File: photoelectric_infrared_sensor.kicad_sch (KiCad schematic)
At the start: 37 parts

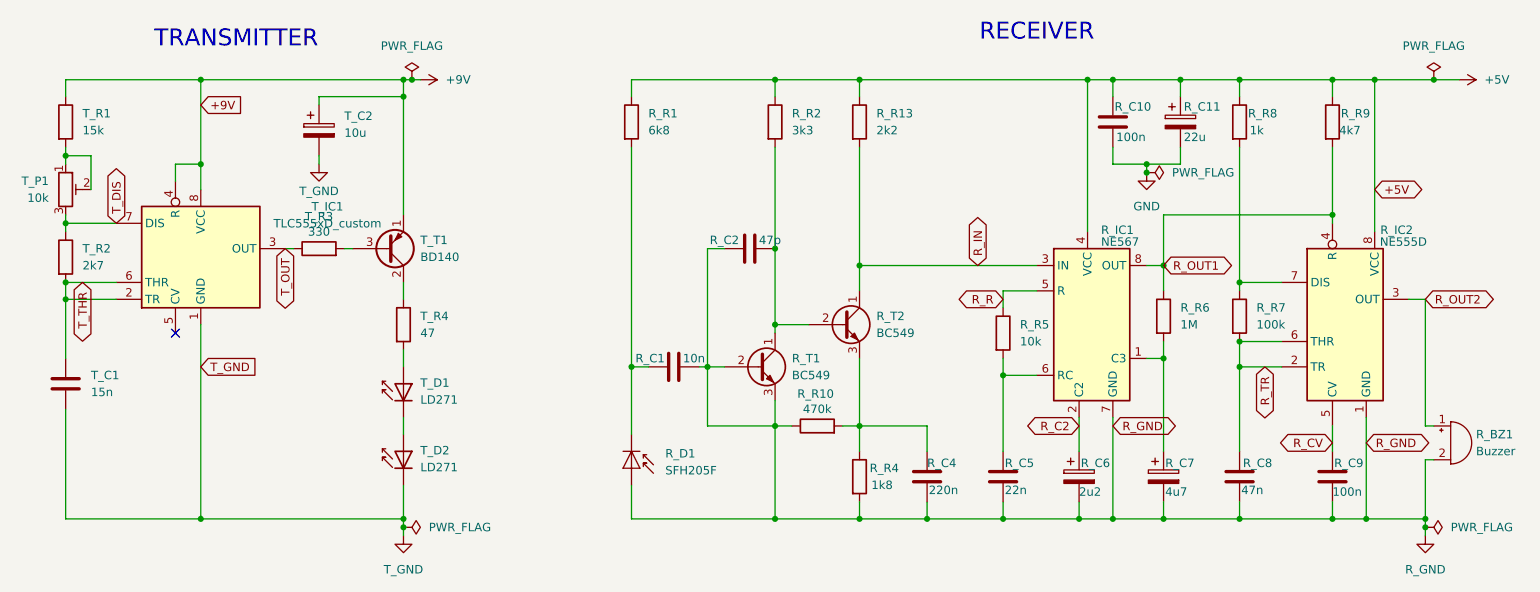
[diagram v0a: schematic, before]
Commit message: added BOM
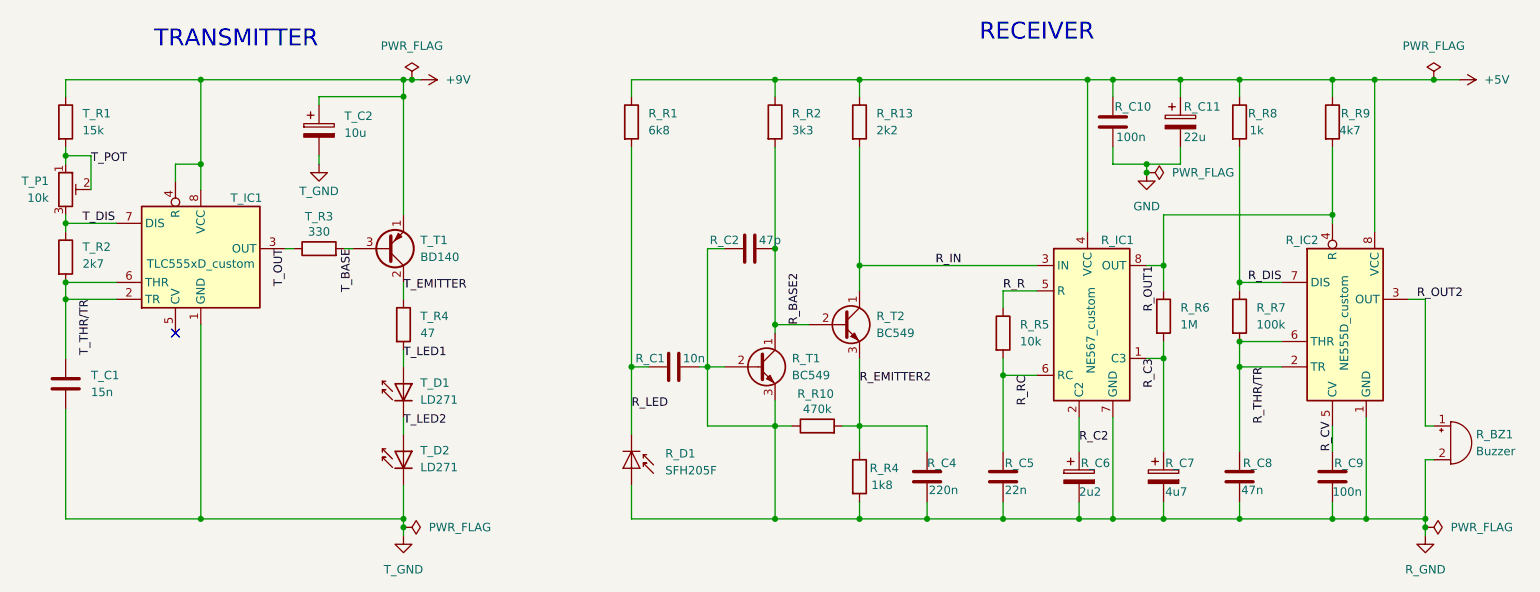
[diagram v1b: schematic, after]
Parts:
- removed R_IC1: NE567, Package_SO:SOIC-8_3.9x4.9mm_P1.27mm, symbol Timer:NE567
- removed R_IC2: NE555D, Package_SO:SOIC-8_3.9x4.9mm_P1.27mm, symbol Timer:NE555D
- added R_IC1: NE567_custom, Package_SO:SOIC-8_3.9x4.9mm_P1.27mm, symbol NE567_custom:NE567_custom
- added R_IC2: NE555D_custom, Package_SO:SOIC-8_3.9x4.9mm_P1.27mm, symbol NE555D_custom:NE555D_custom
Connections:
- net +5V: now also R_IC1.4 (VCC), R_IC2.8 (VCC)
- net R_C2: now also R_IC1.2 (C2)
- net R_CV: now also R_IC2.5 (CV)
- net R_GND: now also R_IC1.7 (GND), R_IC2.1 (GND)
- net R_IN: now also R_IC1.3 (IN)
- net R_OUT1: now also R_IC1.8 (OUT), R_IC2.4 (R)
- net R_OUT2: now also R_IC2.3 (OUT)
- net R_R: now also R_IC1.5 (R)
- net R_EMITTER2: now reaches R_C4.1, R_R10.2, R_R4.1, R_T2.3 (E)
- net R_DIS: now reaches R_R7.1, R_R8.2
- net R_DIS: now also R_IC2.7 (DIS)
- net T_LED2: now reaches T_D1.1 (K), T_D2.2 (A)
- net R_BASE2: now reaches R_C2.2, R_R2.2, R_T1.1 (C), R_T2.2 (B)
- net T_LED1: now reaches T_D1.2 (A), T_R4.2
- net T_BASE: now reaches T_R3.2, T_T1.3 (B)
- net R_RC: now reaches R_C5.1, R_R5.2
- net R_RC: now also R_IC1.6 (RC)
- net T_POT: now reaches T_P1.1, T_P1.2, T_R1.2
- net R_LED: now reaches R_C1.2, R_D1.1 (K), R_R1.2
- net R_C3: now reaches R_C7.1, R_R6.2
- net R_C3: now also R_IC1.1 (C3)
- net T_EMITTER: now reaches T_R4.1, T_T1.2 (C)
- net R_TR renamed R_THR/TR
- net R_THR/TR: now also R_IC2.2 (TR), R_IC2.6 (THR)
- net T_THR renamed T_THR/TR

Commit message: finished schematics
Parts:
- removed T_P1: 10k, Potentiometer_SMD:Potentiometer_Vishay_TS53YJ_Vertical, symbol Device:R_Potentiometer_Trim
- added VR1: PVG5A103C03R00, PVG5A100C03R00, symbol SamacSys_Parts:PVG5A103C03R00
- R_BZ1: footprint Buzzer_Beeper:Buzzer_12x9.5RM7.6 -> CPT-1203-03-SMT-TR:CPT-1203-03-SMT-TR
- R_C1, R_C10, R_C2, R_C4, R_C5, R_C8, R_C9, T_C1: footprint Capacitor_SMD:CP_Elec_4x3 -> Capacitor_SMD:C_0402_1005Metric_Pad0.74x0.62mm_HandSolder
- R_D1: value SFH205F -> BPW34; footprint OptoDevice:Osram_SFH205 -> BPW_34_FAS-Z2:BPW34FASZ
- R_R1, R_R10, R_R13, R_R2, R_R4, R_R5, R_R6, R_R7, R_R8, R_R9, T_R1, T_R2, T_R3: footprint Resistor_SMD:R_0201_0603Metric -> ERJUP6_custom:ERJUP6
- T_C2: footprint Capacitor_SMD:CP_Elec_4x3 -> Capacitor_SMD:CP_Elec_3x5.4
- T_D1, T_D2: value LD271 -> SFH 4851; footprint LED_THT:LED_D5.0mm_IRGrey -> SFH_4851:SFH4851
- T_R4: footprint Resistor_SMD:R_0201_0603Metric -> ERJS1T_U1T__2512_:ERJS1T_U1T__2512_
- T_T1: value BD140 -> BD136
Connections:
- net T_DIS: now also VR1.3 (CW)
- net T_POT: now also VR1.1 (CCW), VR1.2 (WIPER)
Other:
- moved on the sheet: T_C1, T_C2, T_D1, T_D2, T_IC1, T_R1, T_R2, T_R3, T_R4, T_T1

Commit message: added schematics as .pdf
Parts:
- removed VR1: PVG5A103C03R00, PVG5A100C03R00, symbol SamacSys_Parts:PVG5A103C03R00
- added VR1: PVG5A103C03R00, PVG5A100C03R00, symbol PVG5A103C03R00:PVG5A103C03R00
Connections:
- net T_DIS: now also VR1.3 (CW)
- net T_POT: now also VR1.1 (CCW), VR1.2 (WIPER)
